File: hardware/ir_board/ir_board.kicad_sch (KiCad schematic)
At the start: 22 parts, among them J1 Conn_01x05, Q1 IRLML0030, U1 VL53L0CXV0DH1

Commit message: finished schematic for all
Signed-off-by: Vortex-Overdrive <kkurapati10@gmail.com>
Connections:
- net XSHUT: now also R1.2, U1.5 (XSHUT)
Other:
- moved on the sheet: R1
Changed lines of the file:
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@@
 	)
 	(junction
+		(at 63.5 36.83)
+		(diameter 0)
+		(color 0 0 0 0)
+	)
+	(junction
 		(at 33.02 64.77)
 		(diameter 0)
@@
 	(wire
 		(pts
-			(xy 63.5 35.56) (xy 63.5 36.83)
+			(xy 34.29 111.76) (xy 44.45 111.76)
 		)
 		(stroke
@@
 	(wire
 		(pts
-			(xy 34.29 111.76) (xy 44.45 111.76)
+			(xy 63.5 21.59) (xy 63.5 22.86)
 		)
 		(stroke
@@
 	(wire
 		(pts
-			(xy 63.5 24.13) (xy 63.5 27.94)
+			(xy 60.96 36.83) (xy 63.5 36.83)
 		)
 		(stroke
@@
 	(wire
 		(pts
-			(xy 48.26 21.59) (xy 48.26 29.21)
+			(xy 63.5 36.83) (xy 71.12 36.83)
 		)
 		(stroke
@@
 	(wire
 		(pts
-			(xy 118.11 26.67) (xy 127 26.67)
+			(xy 48.26 21.59) (xy 48.26 29.21)
 		)
 		(stroke
@@
 	(wire
 		(pts
-			(xy 106.68 26.67) (xy 106.68 30.48)
+			(xy 118.11 26.67) (xy 127 26.67)
 		)
 		(stroke
@@
 	(wire
 		(pts
-			(xy 175.26 53.34) (xy 175.26 55.88)
+			(xy 106.68 26.67) (xy 106.68 30.48)
 		)
 		(stroke
@@
 	(wire
 		(pts
-			(xy 33.02 64.77) (xy 39.37 64.77)
+			(xy 175.26 53.34) (xy 175.26 55.88)
 		)
 		(stroke
@@
 	(wire
 		(pts
-			(xy 48.26 21.59) (xy 34.29 21.59)
+			(xy 33.02 64.77) (xy 39.37 64.77)
 		)
 		(stroke
@@
 	(wire
 		(pts
-			(xy 60.96 36.83) (xy 63.5 36.83)
+			(xy 48.26 21.59) (xy 34.29 21.59)
 		)
 		(stroke
@@
 	(wire
 		(pts
+			(xy 63.5 30.48) (xy 63.5 36.83)
+		)
+		(stroke
+			(width 0)
+			(type default)
+		)
+	)
+	(wire
+		(pts
 			(xy 34.29 21.59) (xy 34.29 25.4)
 		)
@@
 		)
 	)
+	(label "XSHUT"
+		(at 71.12 36.83 180)
+		(effects
+			(font
+				(size 1.27 1.27)
+			)
+			(justify right bottom)
+		)
+	)
 	(label "GPIO1Conn"
 		(at 95.25 49.53 180)
@@
 	(symbol
 		(lib_id "power:+3.3V")
-		(at 63.5 24.13 0)
+		(at 63.5 21.59 0)
 		(unit 1)
 		(exclude_from_sim no)
@@
 		(dnp no)
 		(property "Reference" "#PWR02"
-			(at 63.5 27.94 0)
+			(at 63.5 25.4 0)
 			(effects
 				(font
@@
 		)
 		(property "Value" "+3.3V"
-			(at 63.5 20.066 0)
+			(at 63.5 17.526 0)
 			(effects
 				(font
@@
 		)
 		(property "Footprint" ""
-			(at 63.5 24.13 0)
+			(at 63.5 21.59 0)
 			(effects
 				(font
@@
 		)
 		(property "Datasheet" ""
-			(at 63.5 24.13 0)
+			(at 63.5 21.59 0)
 			(effects
 				(font
@@
 		)
 		(property "Description" "Power symbol creates a global label with name \"+3.3V\""
-			(at 63.5 24.13 0)
+			(at 63.5 21.59 0)
 			(effects
 				(font
@@
 	(symbol
 		(lib_id "Device:R")
-		(at 63.5 31.75 0)
+		(at 63.5 26.67 0)
 		(unit 1)
 		(exclude_from_sim no)
@@
 		(fields_autoplaced yes)
 		(property "Reference" "R1"
-			(at 66.04 30.4799 0)
+			(at 66.04 25.3999 0)
 			(effects
 				(font
@@
 		)
 		(property "Value" "10k"
-			(at 66.04 33.0199 0)
+			(at 66.04 27.9399 0)
 			(effects
 				(font
@@
 		)
 		(property "Footprint" ""
-			(at 61.722 31.75 90)
+			(at 61.722 26.67 90)
 			(effects
 				(font
@@
 		)
 		(property "Datasheet" "~"
-			(at 63.5 31.75 0)
+			(at 63.5 26.67 0)
 			(effects
 				(font
@@
 		)
 		(property "Description" "Resistor"
-			(at 63.5 31.75 0)
+			(at 63.5 26.67 0)
 			(effects
 				(font

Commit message: small changes
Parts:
- renumbered TP4 to GND_TP1, TP3 to GND_TP2, TP6 to GND_TP3, TP8 to GND_TP4, TP5 to GPIO1_TP, TP1 to SCL_TP, TP2 to SDA_TP, TP7 to XSHUT_TP
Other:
- note added: "n-type mosfet GPIO-1 sends LOW when new measurement taken, which closes the mosfet. When there's no new measurement, the LED will be on."
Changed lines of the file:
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@@
 		)
 	)
+	(text "n-type mosfet\n\nGPIO-1 sends LOW when new measurement\ntaken, which closes the mosfet. When\nthere's no new measurement, the LED\nwill be on. "
+		(exclude_from_sim no)
+		(at 149.098 67.818 0)
+		(effects
+			(font
+				(size 1.27 1.27)
+			)
+			(justify left)
+		)
+	)
 	(text_box "Testpoints + LEDs\n"
 		(exclude_from_sim no)
@@
 		(dnp no)
 		(fields_autoplaced yes)
-		(property "Reference" "TP6"
+		(property "Reference" "GND_TP3"
 			(at 129.54 66.0399 90)
 			(effects
@@
 			(project "ir_board"
 				(path "/9ddf3e21-5052-4e0d-9a65-ef66f95cd91c"
-					(reference "TP6")
+					(reference "GND_TP3")
 					(unit 1)
 				)
@@
 		(dnp no)
 		(fields_autoplaced yes)
-		(property "Reference" "TP1"
+		(property "Reference" "SCL_TP"
 			(at 132.08 25.3999 90)
 			(effects
@@
 			(project ""
 				(path "/9ddf3e21-5052-4e0d-9a65-ef66f95cd91c"
-					(reference "TP1")
+					(reference "SCL_TP")
 					(unit 1)
 				)
@@
 		(dnp no)
 		(fields_autoplaced yes)
-		(property "Reference" "TP5"
+		(property "Reference" "GPIO1_TP"
 			(at 129.54 60.9599 90)
 			(effects
@@
 			(project "ir_board"
 				(path "/9ddf3e21-5052-4e0d-9a65-ef66f95cd91c"
-					(reference "TP5")
+					(reference "GPIO1_TP")
 					(unit 1)
 				)
@@
 		(dnp no)
 		(fields_autoplaced yes)
-		(property "Reference" "TP2"
+		(property "Reference" "SDA_TP"
 			(at 130.81 43.1799 90)
 			(effects
@@
 			(project "ir_board"
 				(path "/9ddf3e21-5052-4e0d-9a65-ef66f95cd91c"
-					(reference "TP2")
+					(reference "SDA_TP")
 					(unit 1)
 				)
@@
 		(dnp no)
 		(fields_autoplaced yes)
-		(property "Reference" "TP3"
+		(property "Reference" "GND_TP2"
 			(at 130.81 48.2599 90)
 			(effects
@@
 			(project "ir_board"
 				(path "/9ddf3e21-5052-4e0d-9a65-ef66f95cd91c"
-					(reference "TP3")
+					(reference "GND_TP2")
 					(unit 1)
 				)
@@
 		(dnp no)
 		(fields_autoplaced yes)
-		(property "Reference" "TP8"
+		(property "Reference" "GND_TP4"
 			(at 129.54 82.5499 90)
 			(effects
@@
 			(project "ir_board"
 				(path "/9ddf3e21-5052-4e0d-9a65-ef66f95cd91c"
-					(reference "TP8")
+					(reference "GND_TP4")
 					(unit 1)
 				)
@@
 		(dnp no)
 		(fields_autoplaced yes)
-		(property "Reference" "TP4"
+		(property "Reference" "GND_TP1"
 			(at 132.08 30.4799 90)
 			(effects
@@
 			(project "ir_board"
 				(path "/9ddf3e21-5052-4e0d-9a65-ef66f95cd91c"
-					(reference "TP4")
+					(reference "GND_TP1")
 					(unit 1)
 				)
@@
 		(dnp no)
 		(fields_autoplaced yes)
-		(property "Reference" "TP7"
+		(property "Reference" "XSHUT_TP"
 			(at 129.54 77.4699 90)
 			(effects
@@
 			(project "ir_board"
 				(path "/9ddf3e21-5052-4e0d-9a65-ef66f95cd91c"
-					(reference "TP7")
+					(reference "XSHUT_TP")
 					(unit 1)
 				)

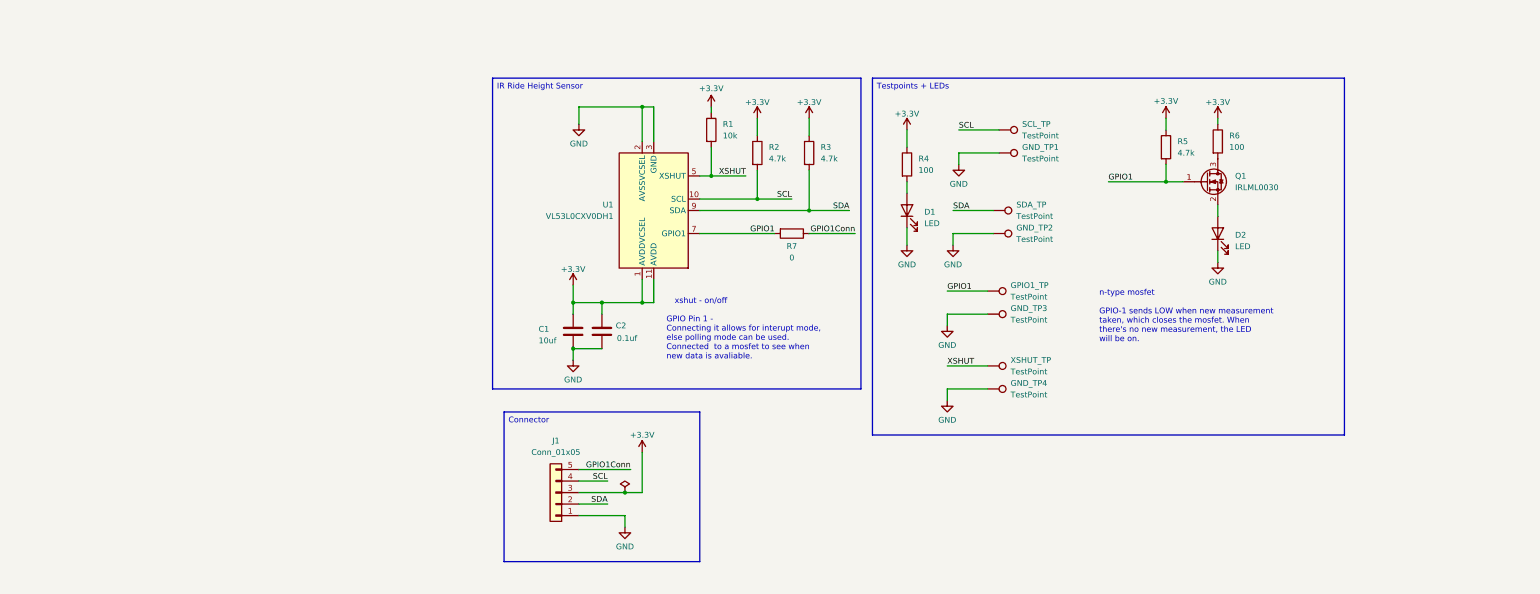
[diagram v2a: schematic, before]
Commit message: added op-amp, finished footprints, new connector, fuse, ldo
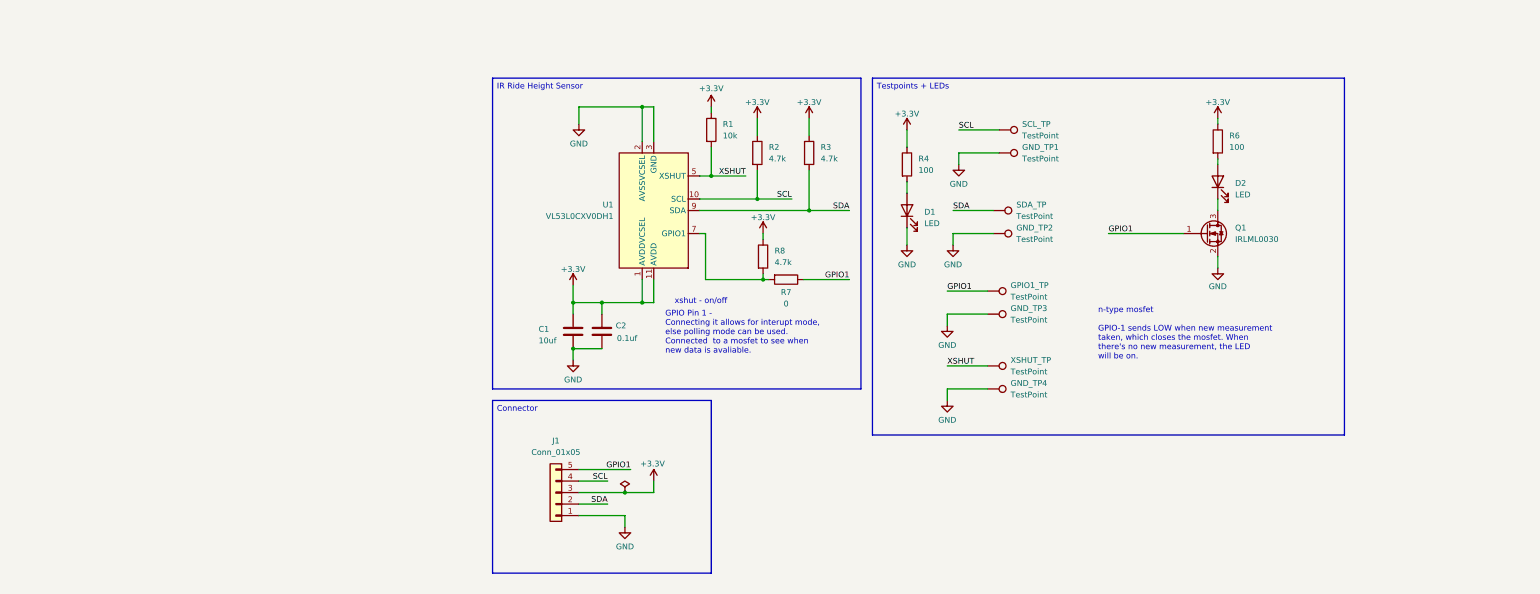
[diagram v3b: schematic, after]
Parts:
- removed R5: 4.7k, symbol Device:R
- added R8: 4.7k, symbol Device:R
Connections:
- net GPIO1Conn is gone; now on net GPIO1: J1.5 (Pin_5), R7.1
- net +3.3V: now also R8.1
- net GND: now also Q1.2 (S); no longer D2.1 (K)
- net GPIO1: no longer R7.2, U1.7 (GPIO1)
- net at D2.2 (A): now also R6.2; no longer Q1.2 (S)
- net at Q1.3 (D): now also D2.1 (K); no longer R6.2
- new net: R7.2, R8.2, U1.7 (GPIO1)
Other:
- moved on the sheet: D2, Q1, R7

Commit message: finished rev a layout for all 3 boards + added cubemx file
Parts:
- removed GND_TP2, GND_TP3, GND_TP4, GPIO1_TP, SCL_TP, SDA_TP: TestPoint, symbol Connector:TestPoint
- removed J1: Conn_01x05, symbol Connector_Generic:Conn_01x05
- added H1, H2, H3, H4: MountingHole, MountingHole:MountingHole_2.2mm_M2, symbol Mechanical:MountingHole
- added J1: Conn_01x04, Connector_PinHeader_2.54mm:PinHeader_1x04_P2.54mm_Vertical, symbol Connector_Generic:Conn_01x04
- added J2: Conn_01x06, Connector_Molex:Molex_Nano-Fit_105310-xx06_2x03_P2.50mm_Vertical, symbol Connector_Generic:Conn_01x06
- C1: footprint (none) -> Capacitor_SMD:C_0603_1608Metric_Pad1.08x0.95mm_HandSolder; P/N (none) -> GRM21BR61H106KE43K
- C2: footprint (none) -> Capacitor_SMD:C_0603_1608Metric_Pad1.08x0.95mm_HandSolder; P/N (none) -> MLASH168SB7104KTNA01
- D1, D2: footprint (none) -> LED_SMD:LED_0603_1608Metric_Pad1.05x0.95mm_HandSolder; P/N (none) -> NCD0603R1
- GND_TP1: footprint (none) -> TestPoint:TestPoint_Pad_1.0x1.0mm
- Q1: P/N (none) -> IRLML0030TRPBF
- R1: footprint (none) -> Resistor_SMD:R_0603_1608Metric_Pad0.98x0.95mm_HandSolder; P/N (none) -> CRCW060310K0FKEI
- R2, R3, R8: footprint (none) -> Resistor_SMD:R_0603_1608Metric_Pad0.98x0.95mm_HandSolder; P/N (none) -> CRCW06034K70FKEA
- R4, R6: value 100 -> 1k; footprint (none) -> Resistor_SMD:R_0603_1608Metric_Pad0.98x0.95mm_HandSolder; P/N (none) -> CRCW06031K00FKEI
- R7: footprint (none) -> Resistor_SMD:R_0603_1608Metric_Pad0.98x0.95mm_HandSolder; P/N (none) -> CRCW06030000Z0EE
- U1: P/N (none) -> 511-VL53L0CXV0DH/1
- XSHUT_TP1: renamed from XSHUT_TP; footprint (none) -> TestPoint:TestPoint_Pad_1.0x1.0mm
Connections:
- net +3.3V: now also J2.4 (Pin_4)
- net GND: now also J1.4 (Pin_4), J2.2 (Pin_2)
- net GPIO1: now also J1.3 (Pin_3), J2.6 (Pin_6)
- net SCL: now also J1.1 (Pin_1), J2.5 (Pin_5)
- net SDA: now also J1.2 (Pin_2), J2.3 (Pin_3)
- no-connect marks 0 -> 1
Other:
- moved on the sheet: XSHUT_TP1

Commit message: finished irboard, tempboard
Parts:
- H1, H2, H3, H4: footprint MountingHole:MountingHole_2.2mm_M2 -> MountingHole:MountingHole_3.2mm_M3

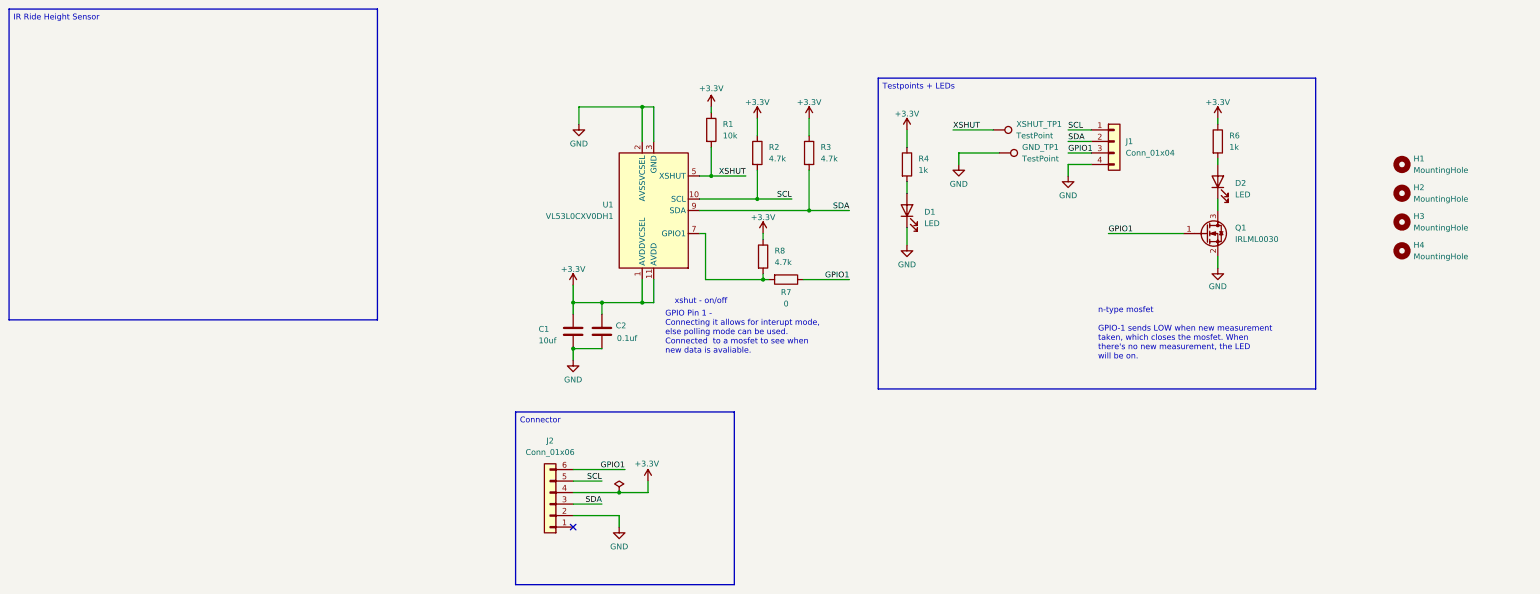
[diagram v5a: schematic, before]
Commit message: finished ir_board, temp_board with horizontal connectors
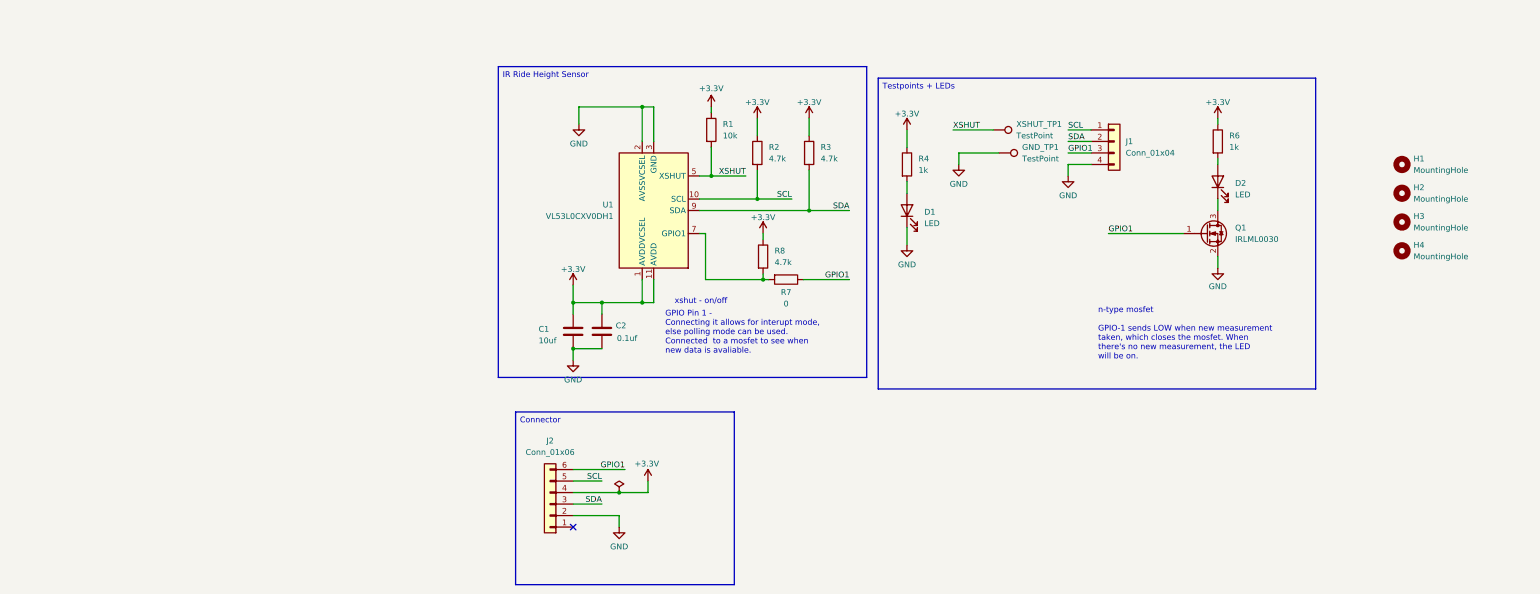
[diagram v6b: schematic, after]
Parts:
- J2: footprint Connector_Molex:Molex_Nano-Fit_105310-xx06_2x03_P2.50mm_Vertical -> Connector_Molex:Molex_Nano-Fit_105314-xx06_2x03_P2.50mm_Horizontal
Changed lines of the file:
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@@
 	(text_box "IR Ride Height Sensor\n"
 		(exclude_from_sim no)
-		(at -91.44 0 0)
+		(at 16.51 12.7 0)
 		(size 81.28 68.58)
 		(margins 0.9525 0.9525 0.9525 0.9525)
@@
 			)
 		)
-		(property "Footprint" "Connector_Molex:Molex_Nano-Fit_105310-xx06_2x03_P2.50mm_Vertical"
+		(property "Footprint" "Connector_Molex:Molex_Nano-Fit_105314-xx06_2x03_P2.50mm_Horizontal"
 			(at 27.94 109.22 0)
 			(effects

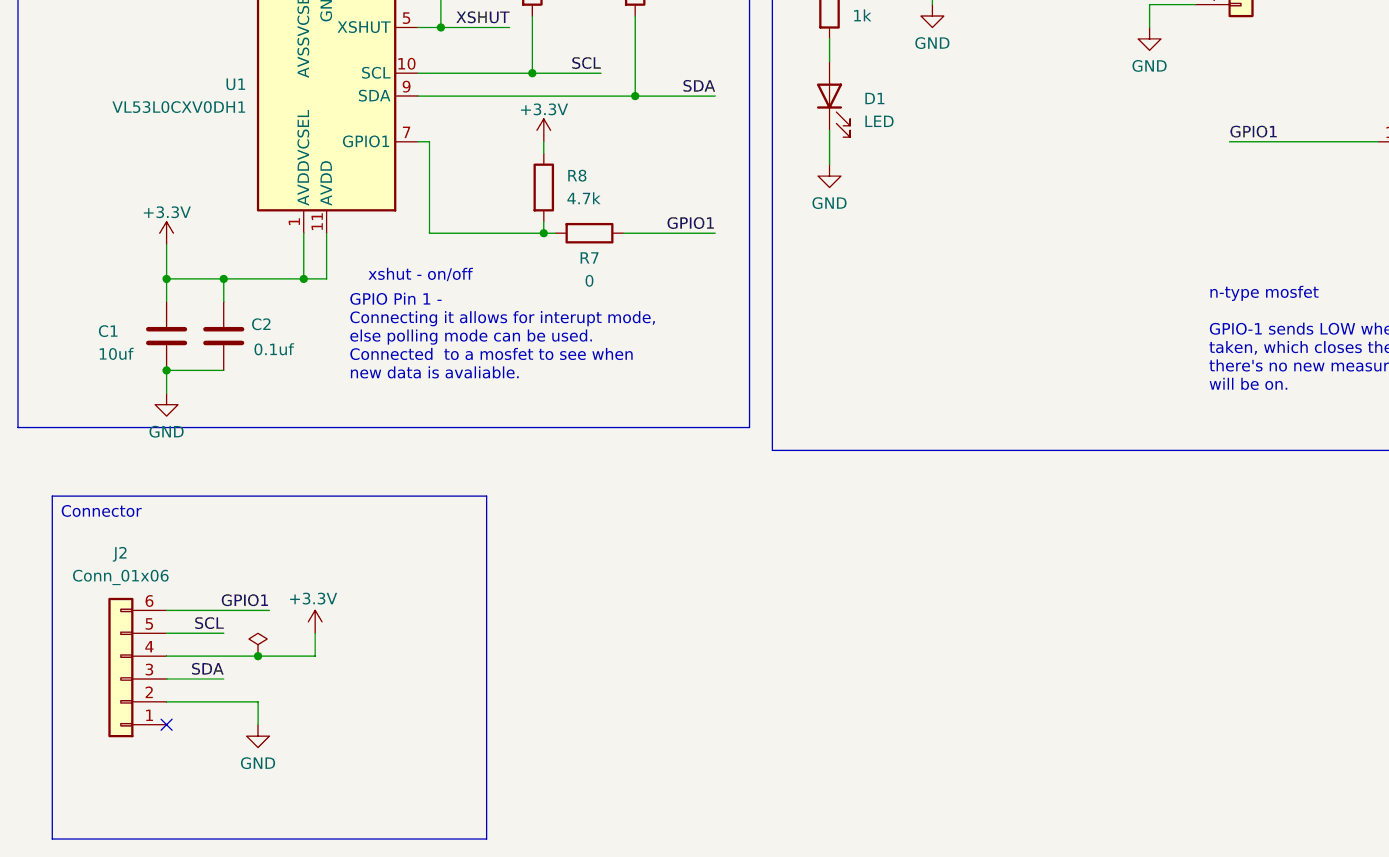
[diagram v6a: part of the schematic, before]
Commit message: .bom files generated, cleaned up pitot board.
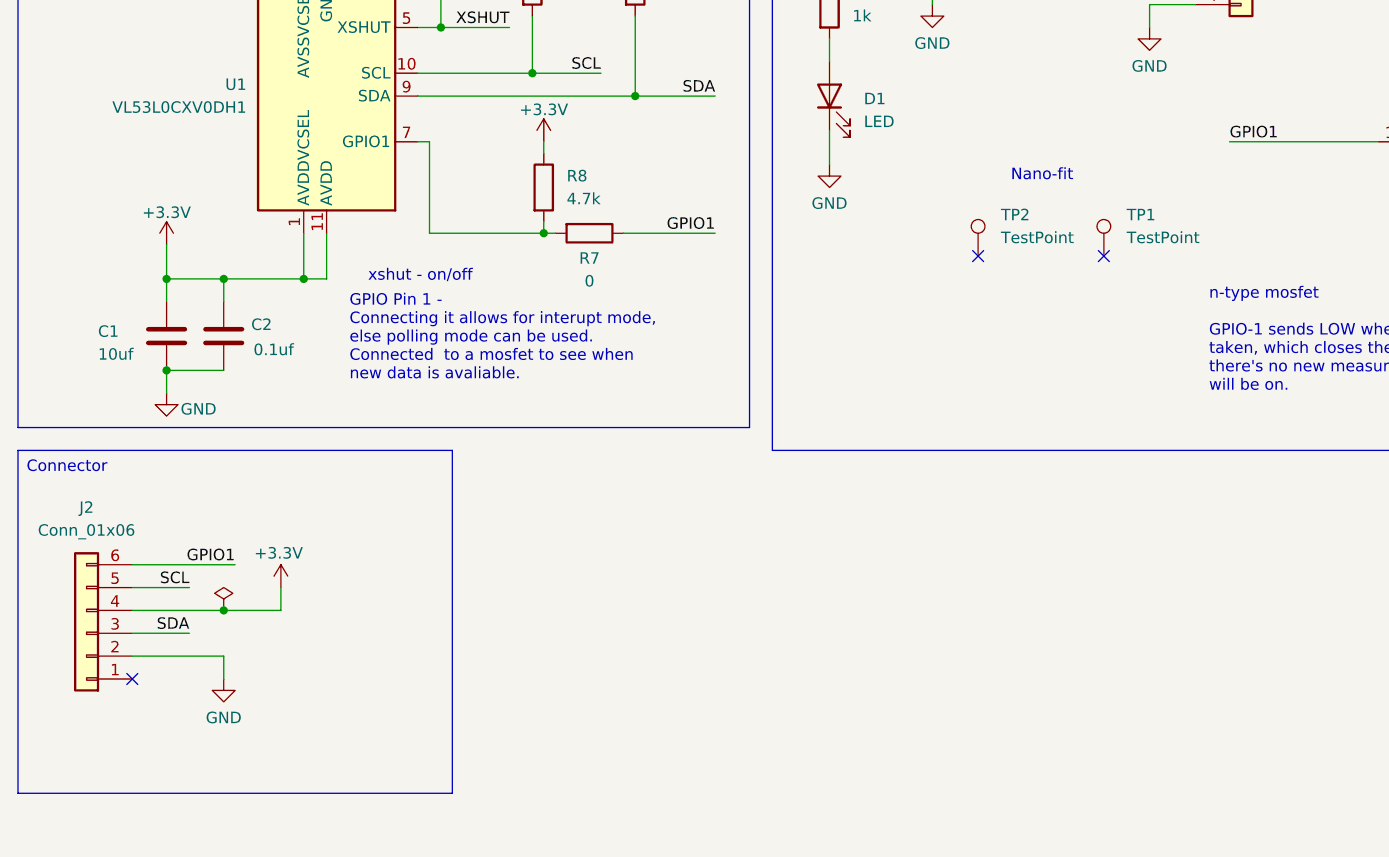
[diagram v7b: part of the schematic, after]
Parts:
- added TP1, TP2: TestPoint, symbol Connector:TestPoint
- J2: P/N WM16880-ND -> 1053141106
- U1: P/N 511-VL53L0CXV0DH/1 -> VL53L0CXV0DH/1
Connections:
- no-connect marks 1 -> 3
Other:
- note added: "Nano-fit"
- moved on the sheet: J2
